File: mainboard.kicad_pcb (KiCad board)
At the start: 2 copper layers, 231.1 x 185.2 mm, 42 parts, among them J1 DRV8833-1, J10 Conn_02x04_Counter_Clockwise, J11 Conn_02x04_Counter_Clockwise, J12 Conn_02x04_Counter_Clockwise, J13 Conn_01x06, J2 DRV8833-0, J3 Conn_01x02, J4 Screw_Terminal_01x06, J5 Screw_Terminal_01x06, J6 VIM4_HEADER, J7 Conn_01x02, J8 Conn_01x02, J9 Conn_02x04_Counter_Clockwise, Q1 2N7000, Q2 2N7000, SW1 RotaryEncoder_Switch, U1 MCP23017_SP, U2 PIC16F819-ISO

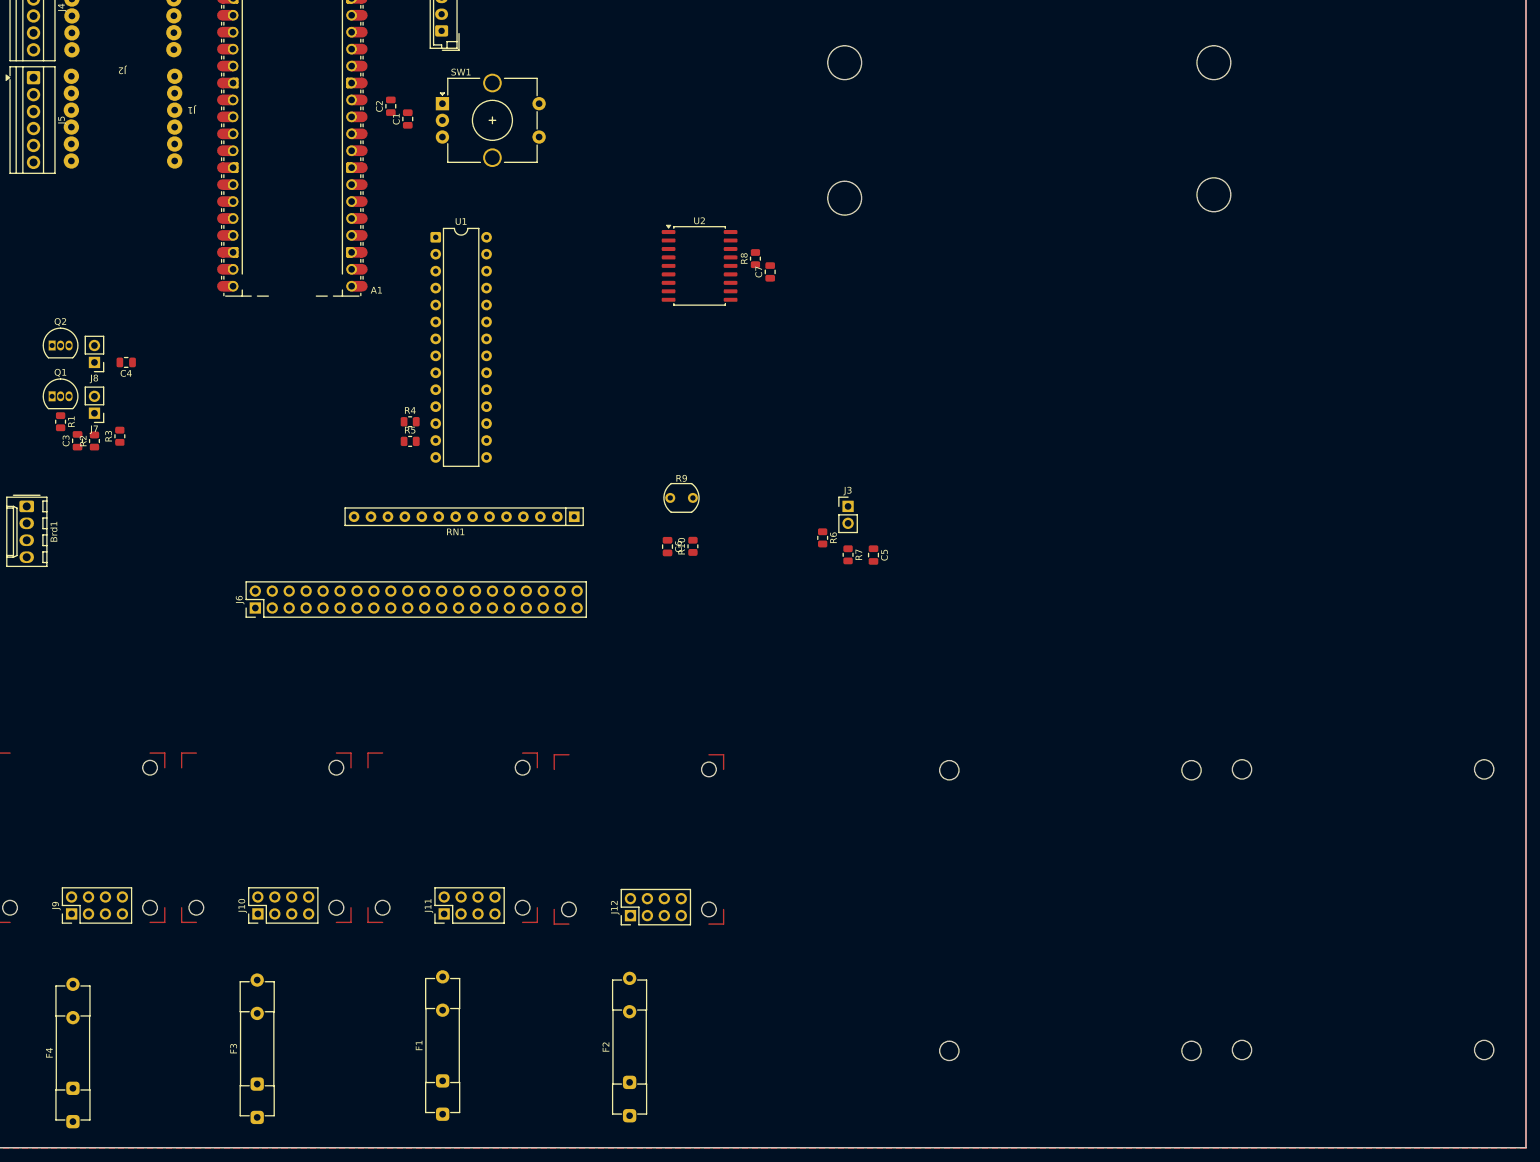
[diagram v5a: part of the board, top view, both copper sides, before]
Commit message: Peripheral footprint blanks and boundaries
Peripheral footprint blanks and boundaries added
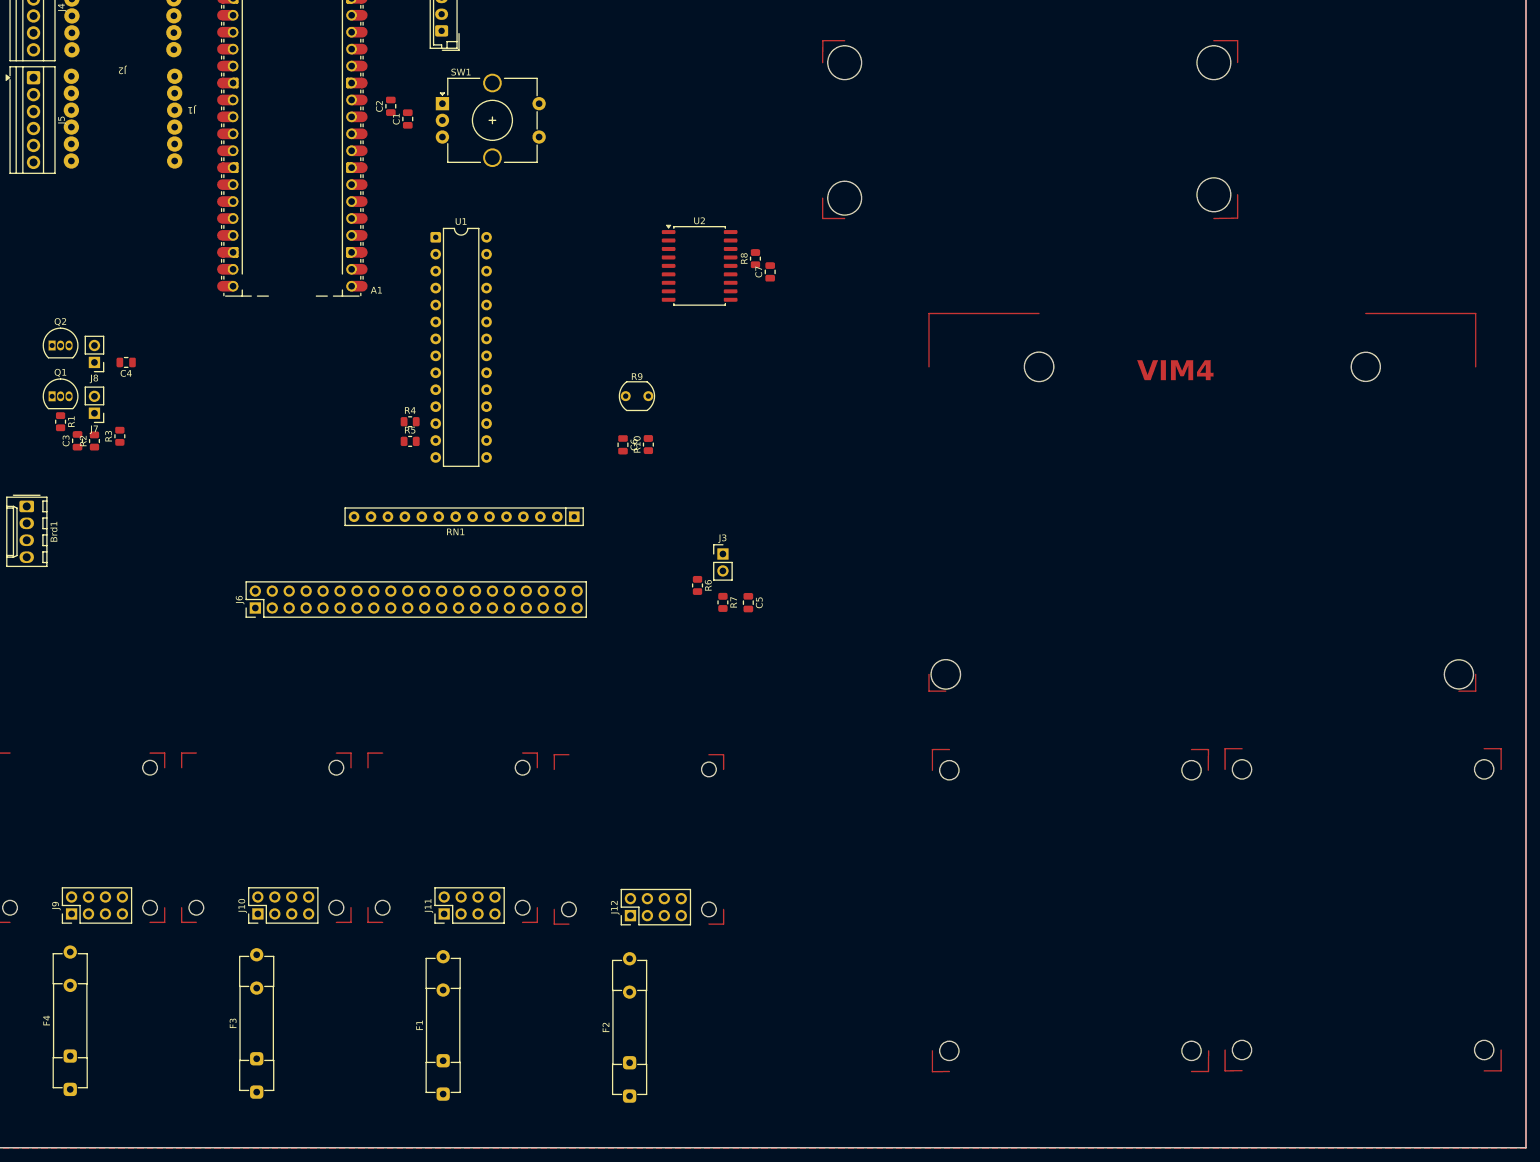
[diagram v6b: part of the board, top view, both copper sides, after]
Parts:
- J13: value Conn_01x06 -> Conn_PCA9685
- moved C5 20.1 mm to (127.3, 116.0)
- moved J3 20.1 mm to (123.5, 108.7)
- moved R7 20.1 mm to (123.5, 116.0)
- moved R6 20.1 mm to (119.7, 113.5)
- moved C6 16.7 mm to (108.5, 92.4)
- moved R10 16.7 mm to (112.3, 92.3)
- moved R9 16.7 mm to (108.9, 85.1)
- moved F4 4.86 mm to (25.6, 189.0)
- moved F3 3.80 mm to (53.5, 189.4)
- moved F1 3.02 mm to (81.5, 189.7)
- moved F2 2.94 mm to (109.5, 190.0)
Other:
- outline, holes or cut-outs redrawn
- board text added: "VIM4"

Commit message: Switches updated
Enumerated all switches in the VIM header and added their respective sub-circuitry. Fixed a few errors I was getting when I updated PCB from schematic.
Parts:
- added C10: 1uF, Capacitor_SMD:C_0805_2012Metric, F.Cu at (274.9, 42.2)
- added C8: 1uF, Capacitor_SMD:C_0805_2012Metric, F.Cu at (274.9, 36.2)
- added C9: 1uF, Capacitor_SMD:C_0805_2012Metric, F.Cu at (274.9, 39.2)
- added J14: Conn_01x02, Connector_PinHeader_2.54mm:PinHeader_1x02_P2.54mm_Vertical, F.Cu at (275.0, 29.8)
- added J15: Conn_01x02, Connector_PinHeader_2.54mm:PinHeader_1x02_P2.54mm_Vertical, F.Cu at (279.6, 29.8)
- added J16: Conn_01x02, Connector_PinHeader_2.54mm:PinHeader_1x02_P2.54mm_Vertical, F.Cu at (284.2, 29.8)
- added R11: 220, Resistor_SMD:R_0805_2012Metric, F.Cu at (270.5, 29.0)
- added R12: 10k, Resistor_SMD:R_0805_2012Metric, F.Cu at (270.5, 32.0)
- added R13: 220, Resistor_SMD:R_0805_2012Metric, F.Cu at (270.5, 34.9)
- added R14: 10k, Resistor_SMD:R_0805_2012Metric, F.Cu at (270.5, 37.9)
- added R15: 220, Resistor_SMD:R_0805_2012Metric, F.Cu at (270.5, 40.8)
- added R16: 10k, Resistor_SMD:R_0805_2012Metric, F.Cu at (270.5, 43.8)
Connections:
- net Net-(RN1-R1) renamed CP-L-ENDSTOP1
- net Net-(RN1-R12) renamed CP-R-ENDSTOP1
- net Net-(RN1-R13) renamed CP-R-ENDSTOP0
- net Net-(RN1-R2) renamed CP-L-ENDSTOP0
- C5 pad 1: SWITCH -> SW-L-A
- R6 pad 2: SWITCH -> SW-L-A
- R7 pad 1: SWITCH -> SW-L-A
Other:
- board size 231.1 x 185.2 mm -> 329.8 x 185.2 mm

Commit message: The Great Simplification
Schematic:
Pico2 added, 12V buck added, Motor-Encoder Interface Added, PIC removed.

*No work yet on PCB, will chip away at orienting objects tomorrow.
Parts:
- removed C3, C4: 1uF, Capacitor_SMD:C_0805_2012Metric
- removed C7: 0.1uF, Capacitor_SMD:C_0805_2012Metric
- removed Q1, Q2: 2N7000, Package_TO_SOT_THT:TO-92_Inline
- removed R1, R8: 10k, Resistor_SMD:R_0805_2012Metric
- removed R2, R3: 220, Resistor_SMD:R_0805_2012Metric
- removed U2: PIC16F819-ISO, Package_SO:SOIC-18W_7.5x11.6mm_P1.27mm
- added A2: RaspberryPi_Pico, Module:RaspberryPi_Pico_Common_Unspecified, F.Cu at (-69.8, 141.7)
- added C10: 1uF, Capacitor_SMD:C_0805_2012Metric, F.Cu at (223.4, 112.4)
- added C5: 1uF, Capacitor_SMD:C_0805_2012Metric, F.Cu at (223.4, 103.4)
- added C8: 1uF, Capacitor_SMD:C_0805_2012Metric, F.Cu at (223.4, 106.4)
- added C9: 1uF, Capacitor_SMD:C_0805_2012Metric, F.Cu at (223.4, 109.4)
- added D1: LED_Small, LED_SMD:LED_0805_2012Metric_Pad1.15x1.40mm_HandSolder, F.Cu at (213.7, 201.5)
- added F5: Fuse, Fuse:Fuseholder_Clip-5x20mm_Schurter_CQM_Inline_P20.60x5.00mm_D1.00mm_Horizontal, F.Cu at (110.9, 279.7)
- added F6: Fuse, Fuse:Fuseholder_Clip-5x20mm_Schurter_CQM_Inline_P20.60x5.00mm_D1.00mm_Horizontal, F.Cu at (139.7, 279.4)
- added J14: Conn_01x02, Connector_PinHeader_2.54mm:PinHeader_1x02_P2.54mm_Vertical, F.Cu at (228.1, 97.0)
- added J15: Conn_01x02, Connector_PinHeader_2.54mm:PinHeader_1x02_P2.54mm_Vertical, F.Cu at (232.7, 97.0)
- added J16: Conn_01x02, Connector_PinHeader_2.54mm:PinHeader_1x02_P2.54mm_Vertical, F.Cu at (237.3, 97.0)
- added J17: Conn_02x04_Counter_Clockwise, Connector_PinHeader_2.54mm:PinHeader_2x04_P2.54mm_Vertical, F.Cu at (111.0, 252.8)
- added J18: Screw_Terminal_01x06, Connector_PinHeader_2.54mm:PinHeader_1x06_P2.54mm_Vertical, F.Cu at (213.6, 185.0)
- added J19: Screw_Terminal_01x06, Connector_PinHeader_2.54mm:PinHeader_1x06_P2.54mm_Vertical, F.Cu at (218.2, 185.0)
- added J20: Screw_Terminal_01x06, Connector_PinHeader_2.54mm:PinHeader_1x06_P2.54mm_Vertical, F.Cu at (222.8, 185.0)
- added J21: Screw_Terminal_01x06, Connector_PinHeader_2.54mm:PinHeader_1x06_P2.54mm_Vertical, F.Cu at (227.4, 185.0)
- added J22: Screw_Terminal_01x06, Connector_PinHeader_2.54mm:PinHeader_1x06_P2.54mm_Vertical, F.Cu at (232.0, 185.0)
- added J23: Screw_Terminal_01x06, Connector_PinHeader_2.54mm:PinHeader_1x06_P2.54mm_Vertical, F.Cu at (236.6, 185.0)
- added J24: Screw_Terminal_01x04, Connector_PinHeader_2.54mm:PinHeader_1x04_P2.54mm_Vertical, F.Cu at (204.4, 202.3)
- added J25: Screw_Terminal_01x02, Connector_PinHeader_2.54mm:PinHeader_1x02_P2.54mm_Vertical, F.Cu at (209.0, 202.3)
- added J26: Conn_02x04_Counter_Clockwise, Connector_PinHeader_2.54mm:PinHeader_2x04_P2.54mm_Vertical, F.Cu at (139.8, 252.9)
- added J3: Conn_01x02, Connector_PinHeader_2.54mm:PinHeader_1x02_P2.54mm_Vertical, F.Cu at (223.5, 97.0)
- added Q3: 2N7000, Package_TO_SOT_THT:TO-92_Inline, F.Cu at (227.6, 105.1)
- added Q4: 2N7000, Package_TO_SOT_THT:TO-92_Inline, F.Cu at (227.6, 110.9)
- added R11: 220, Resistor_SMD:R_0805_2012Metric, F.Cu at (219.0, 102.1)
- added R12: 10k, Resistor_SMD:R_0805_2012Metric, F.Cu at (219.0, 105.1)
- added R13: 220, Resistor_SMD:R_0805_2012Metric, F.Cu at (219.0, 108.0)
- added R14: 220, Resistor_SMD:R_0805_2012Metric, F.Cu at (219.0, 111.0)
- added R15: 10k, Resistor_SMD:R_0805_2012Metric, F.Cu at (219.0, 113.9)
- added R16: 10k, Resistor_SMD:R_0805_2012Metric, F.Cu at (219.0, 116.9)
- added R6: 220, Resistor_SMD:R_0805_2012Metric, F.Cu at (219.0, 96.2)
- added R7: 10k, Resistor_SMD:R_0805_2012Metric, F.Cu at (219.0, 99.2)
- added SW3: SW_SPST, LED_SMD:LED_0805_2012Metric_Pad1.15x1.40mm_HandSolder, F.Cu at (213.7, 204.5)
- J6: footprint Connector_PinHeader_2.54mm:PinHeader_2x20_P2.54mm_Vertical -> Connector_IDC:IDC-Header_2x20_P2.54mm_Latch_Vertical
- J7, J8: value Conn_01x02 -> Screw_Terminal_01x06; footprint Connector_PinHeader_2.54mm:PinHeader_1x02_P2.54mm_Vertical -> Connector_PinHeader_2.54mm:PinHeader_1x06_P2.54mm_Vertical
- SW1: footprint Rotary_Encoder:RotaryEncoder_Alps_EC12E-Switch_Vertical_H20mm_CircularMountingHoles -> Rotary_Encoder:RotaryEncoder_Alps_EC11E-Switch_Vertical_H20mm
- moved J8 208.2 mm to (209.0, 185.0), turned to 0 degrees
- moved J7 200.5 mm to (204.4, 185.0), turned to 0 degrees
- moved F4 168.6 mm to (140.6, 65.7)
- moved J9 168.6 mm to (140.8, 39.4)
- moved F1 93.8 mm to (54.4, 279.6)
- moved F2 93.8 mm to (82.4, 279.9)
- moved F3 93.8 mm to (26.5, 279.3)
- moved J10 93.8 mm to (26.6, 252.5)
- moved J11 93.8 mm to (54.6, 252.5)
- moved J12 93.8 mm to (82.5, 252.8)
- moved J6 4.66 mm to (51.3, 112.7)
- moved J1 2.79 mm to (44.2, 33.1)
- moved J2 2.79 mm to (44.1, 16.4)
- moved J4 2.79 mm to (21.4, 18.0)
- moved J5 2.79 mm to (21.4, 34.9)
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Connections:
- net AGND renamed AGND1
- A1 pad 36: PICO_3V3 -> PICO1_3V3
- Brd1 pad 2: PICO_3V3 -> PICO1_3V3
- C6 pad 2: GND -> AGND2
- J1 pad 3: 12V_BUCK -> 12V_BUCK3
- J12 pad 7: 12V_BUCK -> 12V_BUCK1
- J12 pad 8: 12V_BUCK -> 12V_BUCK1
- J13 pad 5: PICO_3V3 -> PICO1_3V3
- J2 pad 3: 12V_BUCK -> 12V_BUCK3
- J6 pad 22: COLL/SORT(en/dis) -> unconnected-(J6-Pin_22-Pad22)
- J6 pad 30: HEADLIGHTS -> unconnected-(J6-Pin_30-Pad30)
- J6 pad 33: SW-L-A -> BOOM(ext/ret)
- J6 pad 35: SW-L-B -> unconnected-(J6-Pin_35-Pad35)
- J6 pad 36: SW-R-A -> unconnected-(J6-Pin_36-Pad36)
- J6 pad 37: SW-R-B -> unconnected-(J6-Pin_37-Pad37)
- J6 pad 38: unconnected-(J6-Pin_38-Pad38) -> COLL(en/dis)
- J6 pad 39: unconnected-(J6-Pin_39-Pad39) -> SORT(en/dis)
- J7 pad 1: Net-(J7-Pin_1) -> GND
- J7 pad 2: Net-(J7-Pin_2) -> 5V_BUCK
- J8 pad 1: Net-(J8-Pin_1) -> GND
- J8 pad 2: Net-(J8-Pin_2) -> 5V_BUCK
- R4 pad 1: 3v3 -> PICO1_3V3
- R5 pad 1: 3v3 -> PICO1_3V3
- R9 pad 1: 3V_BUCK -> PICO2_3V3
- RN1 pad 10: Net-(RN1-R9) -> unconnected-(RN1-R9-Pad10)
- RN1 pad 11: Net-(RN1-R10) -> unconnected-(RN1-R10-Pad11)
- RN1 pad 12: Net-(RN1-R11) -> unconnected-(RN1-R11-Pad12)
- U1 pad 18: 3v3 -> PICO1_3V3
- U1 pad 3: Net-(RN1-R11) -> unconnected-(U1-GPB2-Pad3)
- U1 pad 4: Net-(RN1-R10) -> unconnected-(U1-GPB3-Pad4)
- U1 pad 5: Net-(RN1-R9) -> unconnected-(U1-GPB4-Pad5)
- U1 pad 7: unconnected-(U1-GPB5-Pad6) -> unconnected-(U1-GPB6-Pad7)
- U1 pad 8: unconnected-(U1-GPB5-Pad6) -> unconnected-(U1-GPB7-Pad8)
- U1 pad 9: 3v3 -> PICO1_3V3
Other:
- board size 329.8 x 185.2 mm -> 220.9 x 240.6 mm
- board text added: "C/S"
- board text added: "MC1"
- board text added: "MC2"
- board text added: "PICO"
- board text removed: "HEADLIGHTS"
- board text removed: "ROBOCLAW"
